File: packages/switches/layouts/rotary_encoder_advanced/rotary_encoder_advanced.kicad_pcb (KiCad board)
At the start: 2 copper layers, 11 parts

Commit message: WIP update switches
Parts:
- C1, C2, C3, C4: footprint atopile:C0402-b3ef17 -> Samsung_Electro_Mechanics_CL05B104KO5NNNC:C0402
- R1, R2, R3, R4, R5, R6: footprint atopile:R0402-56259e -> UNI_ROYAL_0402WGF1002TCE:R0402
- U1: footprint atopile:VSSOP-8_L2.3-W2.0-P0.50-LS3.1-BR-069dfb -> Texas_Instruments_SN74LVC3G14DCUR:VSSOP-8_L2.3-W2.0-P0.50-LS3.1-BR
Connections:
- C2 pad 1: line-3 -> line
- C3 pad 1: line -> line-2
- C4 pad 1: line-1 -> line-5
- R4 pad 2: line-3 -> line
- R5 pad 2: line -> line-2
- R6 pad 2: line-1 -> line-5
- U1 pad 1: line-3 -> line
- U1 pad 2: line-4 -> line-3
- U1 pad 3: line -> line-2
- U1 pad 5: line-2 -> line-4
- U1 pad 6: line-1 -> line-5
- U1 pad 7: line-5 -> line-1
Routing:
- net line-5: track 0.00 -> 2.47 mm
- net line-3: track 2.47 -> 0.00 mm
- net line-2: track 0.00 -> 2.47 mm
- net line-1: track 2.47 -> 0.00 mm
- net gnd: vias 1 -> 0
- net (no net): vias 0 -> 1

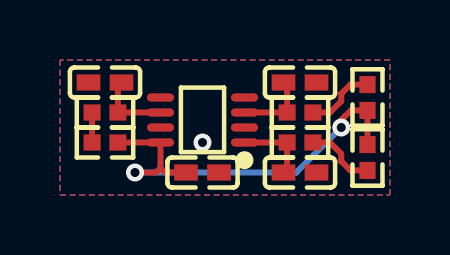
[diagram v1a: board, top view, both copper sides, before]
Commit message: Manually fix fp lib tables
fix some small bugs
fix package only modules (e.g. logos)
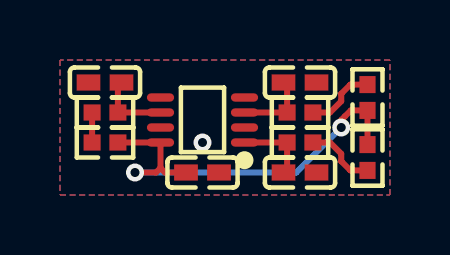
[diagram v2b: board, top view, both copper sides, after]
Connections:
- C4 pad 1: line-5 -> line-4
- R6 pad 2: line-5 -> line-4
- U1 pad 2: line-3 -> line-5
- U1 pad 5: line-4 -> line-1
- U1 pad 6: line-5 -> line-4
- U1 pad 7: line-1 -> line-3
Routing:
- net line-5: track 2.47 -> 0.00 mm
- net line-4: track 0.00 -> 2.47 mm

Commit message: Update 3D model locations
fix missing renders
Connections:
- C2 pad 1: line -> line-2
- C3 pad 1: line-2 -> line-3
- C4 pad 1: line-4 -> line
- R4 pad 2: line -> line-2
- R5 pad 2: line-2 -> line-3
- R6 pad 2: line-4 -> line
- U1 pad 1: line -> line-2
- U1 pad 3: line-2 -> line-3
- U1 pad 6: line-4 -> line
- U1 pad 7: line-3 -> line-4
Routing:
- net line-4: track 2.47 -> 0.00 mm
- net line-3: track 0.00 -> 2.47 mm

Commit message: rebuild all packages & regenerate images of changed layouts (silk)
Add new scripts for version bump and build (based on atopile/packages)
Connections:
- C4 pad 1: line -> line-4
- R6 pad 2: line -> line-4
- U1 pad 6: line -> line-4
- U1 pad 7: line-4 -> line
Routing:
- net line-4: track 0.00 -> 2.47 mm
- net line: track 2.47 -> 0.00 mm
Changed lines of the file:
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@@
     (net 3 "switch")
     (net 4 "line-5")
-    (net 5 "line-4")
-    (net 6 "line")
+    (net 5 "line")
+    (net 6 "line-4")
     (net 7 "line-2")
     (net 8 "gnd")
@@
             )
         )
-        (property "checksum" "8fe27ce2e757dbc35ff8100cb6c40fb5791156bc33545c3a51c757caa1554bcb"
+        (property "checksum" "5bc2e85f7d6a55467344518b833cbc1029e24c207d82b4661305ac8c8f926cf4"
             (at 0 0 0)
             (layer "User.9")
@@
             )
         )
-        (property "__atopile_lib_fp_hash__" "8e585a37-098d-744f-e5aa-b05e5b0b0a58"
+        (property "__atopile_lib_fp_hash__" "51e51474-5d98-1538-1722-13434559b925"
             (at 0 0 0)
             (layer "User.9")
@@
             )
         )
-        (property "checksum" "7c49f9e95a1fd3ac3eafcea64d23dc5908f14bc00c38d701630da2a03cad9033"
+        (property "checksum" "292440642cb4b84e315b23ac32b880ad69d295944f10fab68c014ca3e09d58d5"
             (at 0 0 0)
             (layer "User.9")
@@
             )
         )
-        (property "__atopile_lib_fp_hash__" "3f6d1ec4-0582-a9d7-ce2d-dcf759d8a3ed"
+        (property "__atopile_lib_fp_hash__" "6b8cc7a6-5fdc-33a2-4be0-6225ec39a748"
             (at 0 0 0)
             (layer "User.9")
@@
             )
         )
-        (property "checksum" "8fe27ce2e757dbc35ff8100cb6c40fb5791156bc33545c3a51c757caa1554bcb"
+        (property "checksum" "5bc2e85f7d6a55467344518b833cbc1029e24c207d82b4661305ac8c8f926cf4"
             (at 0 0 0)
             (layer "User.9")
@@
             )
         )
-        (property "__atopile_lib_fp_hash__" "8e585a37-098d-744f-e5aa-b05e5b0b0a58"
+        (property "__atopile_lib_fp_hash__" "51e51474-5d98-1538-1722-13434559b925"
             (at 0 0 0)
             (layer "User.9")
@@
             (size 0.57 0.54)
             (layers "F.Cu" "F.Paste" "F.Mask")
-            (net 6 "line")
+            (net 6 "line-4")
         )
         (pad "1" smd rect
@@
             )
         )
-        (property "checksum" "8fe27ce2e757dbc35ff8100cb6c40fb5791156bc33545c3a51c757caa1554bcb"
+        (property "checksum" "5bc2e85f7d6a55467344518b833cbc1029e24c207d82b4661305ac8c8f926cf4"
             (at 0 0 0)
             (layer "User.9")
@@
             )
         )
-        (property "__atopile_lib_fp_hash__" "8e585a37-098d-744f-e5aa-b05e5b0b0a58"
+        (property "__atopile_lib_fp_hash__" "51e51474-5d98-1538-1722-13434559b925"
             (at 0 0 0)
             (layer "User.9")
@@
             (size 0.28 0.91)
             (layers "F.Cu" "F.Mask" "F.Paste")
-            (net 6 "line")
+            (net 6 "line-4")
         )
         (pad "7" smd oval
@@
             (size 0.28 0.91)
             (layers "F.Cu" "F.Mask" "F.Paste")
-            (net 5 "line-4")
+            (net 5 "line")
         )
         (pad "8" smd oval
@@
             )
         )
-        (property "checksum" "7c49f9e95a1fd3ac3eafcea64d23dc5908f14bc00c38d701630da2a03cad9033"
+        (property "checksum" "292440642cb4b84e315b23ac32b880ad69d295944f10fab68c014ca3e09d58d5"
             (at 0 0 0)
             (layer "User.9")
@@
             )
         )
-        (property "__atopile_lib_fp_hash__" "3f6d1ec4-0582-a9d7-ce2d-dcf759d8a3ed"
+        (property "__atopile_lib_fp_hash__" "6b8cc7a6-5fdc-33a2-4be0-6225ec39a748"
             (at 0 0 0)
             (layer "User.9")
@@
             )
         )
-        (property "checksum" "8fe27ce2e757dbc35ff8100cb6c40fb5791156bc33545c3a51c757caa1554bcb"
+        (property "checksum" "5bc2e85f7d6a55467344518b833cbc1029e24c207d82b4661305ac8c8f926cf4"
             (at 0 0 0)
             (layer "User.9")
@@
             )
         )
-        (property "__atopile_lib_fp_hash__" "8e585a37-098d-744f-e5aa-b05e5b0b0a58"
+        (property "__atopile_lib_fp_hash__" "51e51474-5d98-1538-1722-13434559b925"
             (at 0 0 0)
             (layer "User.9")
@@
             )
         )
-        (property "checksum" "7c49f9e95a1fd3ac3eafcea64d23dc5908f14bc00c38d701630da2a03cad9033"
+        (property "checksum" "292440642cb4b84e315b23ac32b880ad69d295944f10fab68c014ca3e09d58d5"
             (at 0 0 0)
             (layer "User.9")
@@
             )
         )
-        (property "__atopile_lib_fp_hash__" "3f6d1ec4-0582-a9d7-ce2d-dcf759d8a3ed"
+        (property "__atopile_lib_fp_hash__" "6b8cc7a6-5fdc-33a2-4be0-6225ec39a748"
             (at 0 0 0)
             (layer "User.9")
@@
             )
         )
-        (property "checksum" "8fe27ce2e757dbc35ff8100cb6c40fb5791156bc33545c3a51c757caa1554bcb"
+        (property "checksum" "5bc2e85f7d6a55467344518b833cbc1029e24c207d82b4661305ac8c8f926cf4"
             (at 0 0 0)
             (layer "User.9")
@@
             )
         )
-        (property "__atopile_lib_fp_hash__" "8e585a37-098d-744f-e5aa-b05e5b0b0a58"
+        (property "__atopile_lib_fp_hash__" "51e51474-5d98-1538-1722-13434559b925"
             (at 0 0 0)
             (layer "User.9")
@@
             )
         )
-        (property "checksum" "7c49f9e95a1fd3ac3eafcea64d23dc5908f14bc00c38d701630da2a03cad9033"
+        (property "checksum" "292440642cb4b84e315b23ac32b880ad69d295944f10fab68c014ca3e09d58d5"
             (at 0 0 0)
             (layer "User.9")
@@
             )
         )
-        (property "__atopile_lib_fp_hash__" "3f6d1ec4-0582-a9d7-ce2d-dcf759d8a3ed"
+        (property "__atopile_lib_fp_hash__" "6b8cc7a6-5fdc-33a2-4be0-6225ec39a748"
             (at 0 0 0)
             (layer "User.9")
@@
             (size 0.79 0.54)
             (layers "F.Cu" "F.Paste" "F.Mask")
-            (net 6 "line")
+            (net 6 "line-4")
         )
         (model "${KIPRJMOD}/../../parts/Samsung_Electro_Mechanics_CL05B104KO5NNNC/C0402_L1.0-W0.5-H0.5.step"
@@
             )
         )
-        (property "checksum" "8fe27ce2e757dbc35ff8100cb6c40fb5791156bc33545c3a51c757caa1554bcb"
+        (property "checksum" "5bc2e85f7d6a55467344518b833cbc1029e24c207d82b4661305ac8c8f926cf4"
             (at 0 0 0)
             (layer "User.9")
@@
             )
         )
-        (property "__atopile_lib_fp_hash__" "8e585a37-098d-744f-e5aa-b05e5b0b0a58"
-            (at 0 0 0)
-            (layer "User.9")
+        (property "__atopile_lib_fp_hash__" "51e51474-5d98-1538-1722-13434559b925"
+            (at 0 0 0)
+            (layer "User.9")
